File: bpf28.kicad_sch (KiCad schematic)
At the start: 39 parts

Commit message: 部品定数を入力　ただし未評価
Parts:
- C101, C130: value 10p -> NM
- C102, C129: value 10p -> 4700p
- C103, C105, C107, C109, C111, C113, C115, C117, C119, C121, C123, C125, C127: value 1p -> NM
- C104, C110, C126, C128: value 10p -> 330p
- C106, C120: value 10p -> 180p
- C114, C118: value 10p -> 150p
- L103, L105: value 10n -> NM
- L104, L106: value 1u -> 100n
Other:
- note added: "3t D8.0mm L2.1mm"
- note added: "Butterworth 24M-34M 171p, 79p, 197p"
- company: (none) -> JK1MLY / PRUG
- title: (none) -> FM QRP TRCV

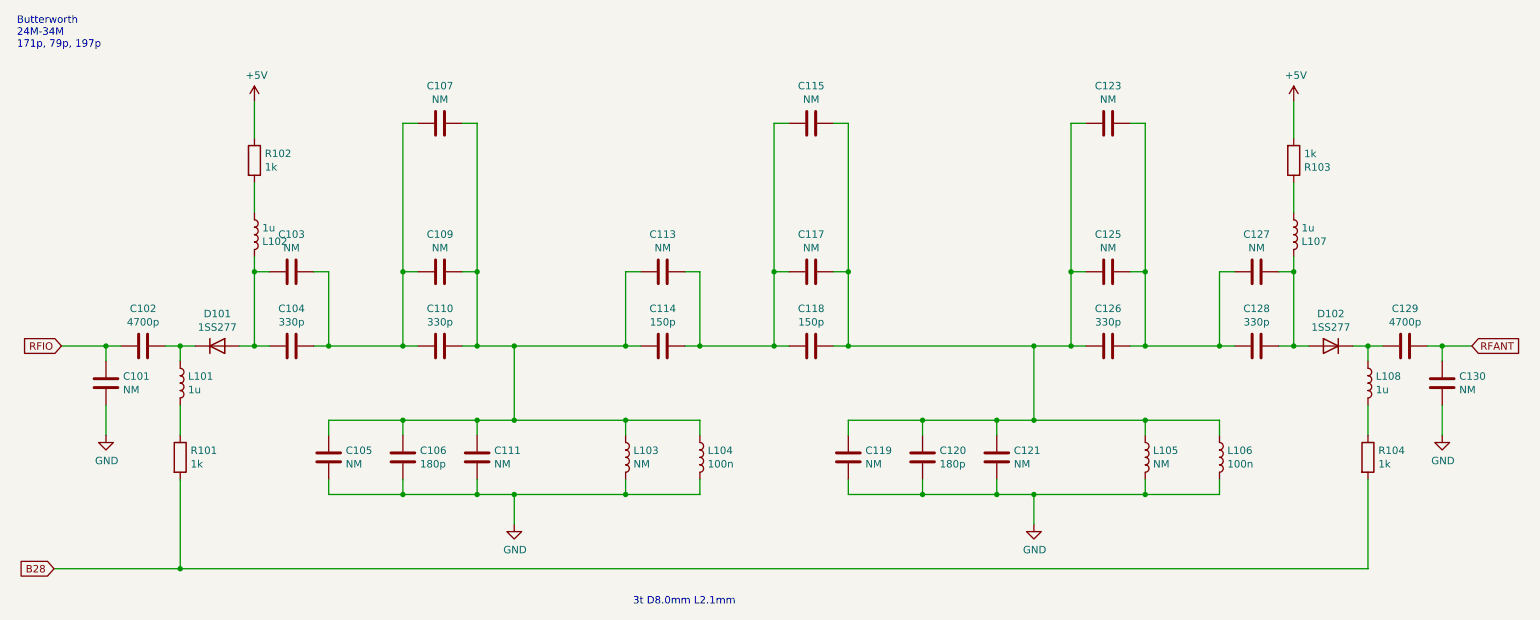
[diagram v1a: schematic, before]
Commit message: Add files via upload
フィルタ回路変更とジャンパクリーン
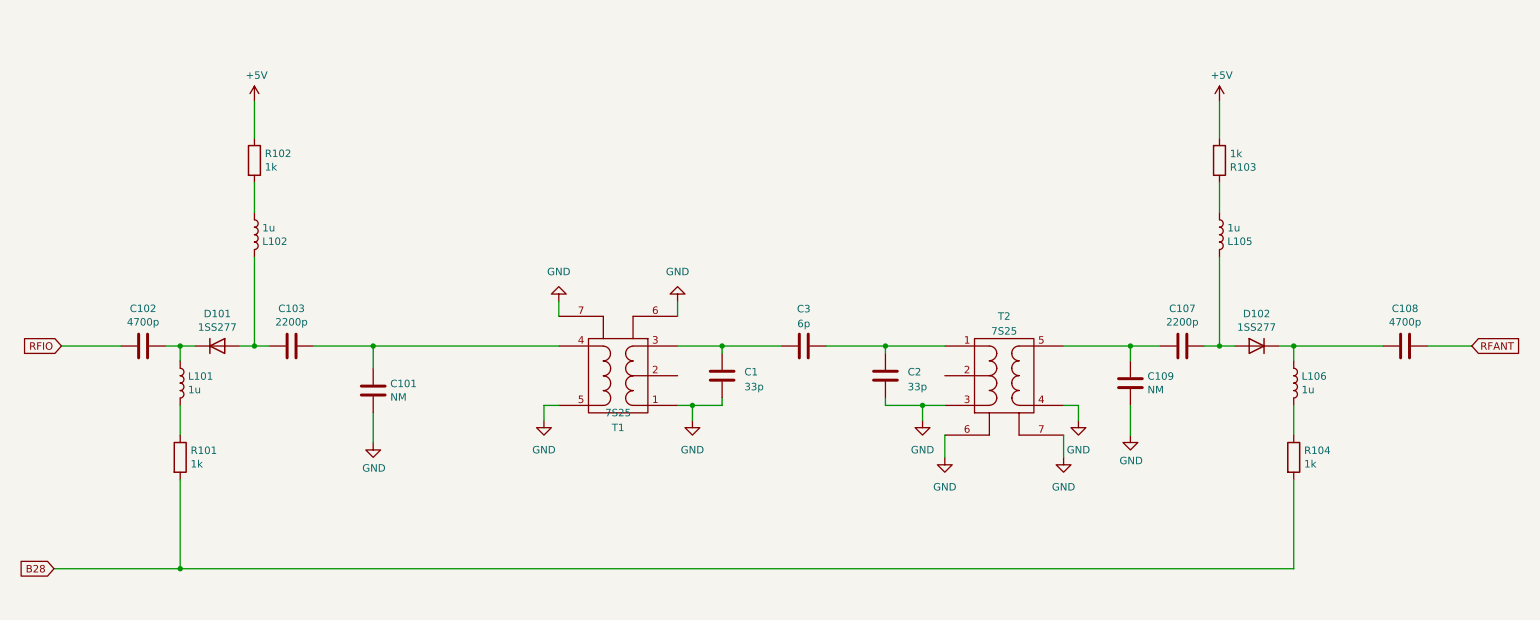
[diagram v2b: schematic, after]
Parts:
- removed C103, C105, C107, C109, C111, C113, C115, C117, C119, C121, C123, C125, C127: NM, digikey-footprints:0603, symbol Device:C
- removed C106, C120: 180p, Capacitor_THT:C_Disc_D3.4mm_W2.1mm_P2.50mm, symbol Device:C
- removed C110, C126: 330p, Capacitor_THT:C_Disc_D3.4mm_W2.1mm_P2.50mm, symbol Device:C
- removed C114, C118: 150p, Capacitor_THT:C_Disc_D3.4mm_W2.1mm_P2.50mm, symbol Device:C
- removed L103, L105: NM, Inductor_SMD:L_Murata_LQH2MCNxxxx02_2.0x1.6mm, symbol Device:L
- removed L104, L106: 100n, Resistor_THT:R_Axial_DIN0204_L3.6mm_D1.6mm_P5.08mm_Horizontal, symbol Device:L
- added C1, C2: 33p, Capacitor_THT:C_Disc_D3.0mm_W2.0mm_P2.50mm, symbol Device:C
- added C3: 6p, Capacitor_THT:C_Disc_D3.0mm_W2.0mm_P2.50mm, symbol Device:C
- added T1, T2: 7S25, usr-Library:coil_7mm, symbol Usr_Library:Transformer_SP_1S
- C103: renamed from C104; value 330p -> 2200p
- C107: renamed from C128; value 330p -> 2200p
- renumbered C129 to C108, C130 to C109, L107 to L105, L108 to L106
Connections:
- net GND: now also C1.2, C2.2, T1.1 (PR1), T1.5 (S2), T1.6 (G1), T1.7 (G2), T2.3 (PR2), T2.4 (S1), T2.6 (G1), T2.7 (G2)
- net RFANT: no longer C109.1
- net RFIO: no longer C101.1
- net at C103.2: now also C101.1, T1.4 (S1)
- net at C107.1: now also C109.1, T2.5 (S2)
- new net: C2.1, C3.1, T2.1 (PR1)
- new net: C1.1, C3.2, T1.3 (PR2)
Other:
- note removed: "3t D8.0mm L2.1mm"
- note removed: "Butterworth 24M-34M 171p, 79p, 197p"
- moved on the sheet: C101, C107, C109, D102, L105, L106, R103, R104

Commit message: アップデート
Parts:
- added R105: 1k, Resistor_THT:R_Axial_DIN0207_L6.3mm_D2.5mm_P2.54mm_Vertical, symbol Device:R
- D101, D102: footprint Diode_THT:D_A-405_P2.54mm_Vertical_AnodeUp -> Diode_THT:D_T-1_P5.08mm_Horizontal
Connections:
- net +5V: now also R103.1, R105.1; no longer R103.2
- net B28: now also R105.2
- net at L105.2: now also R103.2; no longer R103.1
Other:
- note added: "100p 7.5T 100p 560p 100p 7.5T 100p"
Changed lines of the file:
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@@
   (junction (at 228.6 76.2) (diameter 0) (color 0 0 0 0)
   )
+  (junction (at 39.37 114.3) (diameter 0) (color 0 0 0 0)
+  )
   (junction (at 138.43 86.36) (diameter 0) (color 0 0 0 0)
   )
@@
     (stroke (width 0) (type default))
   )
+  (wire (pts (xy 39.37 95.25) (xy 39.37 101.6))
+    (stroke (width 0) (type default))
+  )
   (wire (pts (xy 177.8 86.36) (xy 177.8 88.9))
     (stroke (width 0) (type default))
@@
     (stroke (width 0) (type default))
   )
+  (wire (pts (xy 39.37 109.22) (xy 39.37 114.3))
+    (stroke (width 0) (type default))
+  )
   (wire (pts (xy 135.89 68.58) (xy 135.89 71.12))
     (stroke (width 0) (type default))
@@
     (stroke (width 0) (type default))
   )
+  (wire (pts (xy 39.37 114.3) (xy 29.21 114.3))
+    (stroke (width 0) (type default))
+  )
   (wire (pts (xy 143.51 76.2) (xy 153.67 76.2))
     (stroke (width 0) (type default))
@@
     (stroke (width 0) (type default))
   )
-  (wire (pts (xy 50.8 114.3) (xy 29.21 114.3))
+  (wire (pts (xy 50.8 114.3) (xy 39.37 114.3))
     (stroke (width 0) (type default))
   )
@@
   (wire (pts (xy 241.3 76.2) (xy 241.3 78.74))
     (stroke (width 0) (type default))
+  )
+  (text "100p 7.5T 100p 560p 100p 7.5T 100p" (at 118.11 45.72 0)
+    (effects (font (size 1.27 1.27)) (justify left bottom))
   )
   (global_label "B28" (shape input) (at 29.21 114.3 180) (fields_autoplaced)
@@
       (effects (font (size 1.27 1.27)))
     )
-    (property "Footprint" "Diode_THT:D_A-405_P2.54mm_Vertical_AnodeUp" (at 57.15 76.2 0)
+    (property "Footprint" "Diode_THT:D_T-1_P5.08mm_Horizontal" (at 57.15 76.2 0)
       (effects (font (size 1.27 1.27)) hide)
     )
@@
       (effects (font (size 1.27 1.27)))
     )
-    (property "Footprint" "Diode_THT:D_A-405_P2.54mm_Vertical_AnodeUp" (at 234.95 76.2 0)
+    (property "Footprint" "Diode_THT:D_T-1_P5.08mm_Horizontal" (at 234.95 76.2 0)
       (effects (font (size 1.27 1.27)) hide)
     )
@@
     )
   )
-  (symbol (lib_id "Device:R") (at 228.6 44.45 0) (mirror x) (unit 1)
-    (in_bom yes) (on_board yes) (dnp no)
-    (property "Reference" "R103" (at 230.378 45.6184 0)
-      (effects (font (size 1.27 1.27)) (justify left))
-    )
-    (property "Value" "1k" (at 230.378 43.307 0)
-      (effects (font (size 1.27 1.27)) (justify left))
-    )
-    (property "Footprint" "Resistor_THT:R_Axial_DIN0207_L6.3mm_D2.5mm_P2.54mm_Vertical" (at 226.822 44.45 90)
+  (symbol (lib_id "Device:R") (at 228.6 44.45 0) (mirror y) (unit 1)
+    (in_bom yes) (on_board yes) (dnp no)
+    (property "Reference" "R103" (at 226.822 43.2816 0)
+      (effects (font (size 1.27 1.27)) (justify left))
+    )
+    (property "Value" "1k" (at 226.822 45.593 0)
+      (effects (font (size 1.27 1.27)) (justify left))
+    )
+    (property "Footprint" "Resistor_THT:R_Axial_DIN0207_L6.3mm_D2.5mm_P2.54mm_Vertical" (at 230.378 44.45 90)
       (effects (font (size 1.27 1.27)) hide)
     )
@@
         (path "/6d1d60ff-408a-47a7-892f-c5cf9ef6ca75/00000000-0000-0000-0000-000061d100f6"
           (reference "#PWR0110") (unit 1)
+        )
+      )
+    )
+  )
+  (symbol (lib_id "power:+5V") (at 39.37 95.25 0) (unit 1)
+    (in_bom yes) (on_board yes) (dnp no)
+    (property "Reference" "#PWR054" (at 39.37 99.06 0)
+      (effects (font (size 1.27 1.27)) hide)
+    )
+    (property "Value" "+5V" (at 39.751 90.8558 0)
+      (effects (font (size 1.27 1.27)))
+    )
+    (property "Footprint" "" (at 39.37 95.25 0)
+      (effects (font (size 1.27 1.27)) hide)
+    )
+    (property "Datasheet" "" (at 39.37 95.25 0)
+      (effects (font (size 1.27 1.27)) hide)
+    )
+    (pin "1")
+    (instances
+      (project "fm_qrp2"
+        (path "/6d1d60ff-408a-47a7-892f-c5cf9ef6ca75/00000000-0000-0000-0000-000061d100f6"
+          (reference "#PWR054") (unit 1)
         )
       )
@@
         )
       )
+    )
+  )
+  (symbol (lib_id "Device:R") (at 39.37 105.41 0) (unit 1)
+    (in_bom yes) (on_board yes) (dnp no)
+    (property "Reference" "R105" (at 41.148 104.2416 0)
+      (effects (font (size 1.27 1.27)) (justify left))
+    )
+    (property "Value" "1k" (at 41.148 106.553 0)
+      (effects (font (size 1.27 1.27)) (justify left))
+    )
+    (property "Footprint" "Resistor_THT:R_Axial_DIN0207_L6.3mm_D2.5mm_P2.54mm_Vertical" (at 37.592 105.41 90)
+      (effects (font (size 1.27 1.27)) hide)
+    )
+    (property "Datasheet" "~" (at 39.37 105.41 0)
+      (effects (font (size 1.27 1.27)) hide)
+    )
+    (pin "1")
+    (pin "2")
+    (instances
+      (project "fm_qrp2"
+        (path "/6d1d60ff-408a-47a7-892f-c5cf9ef6ca75/00000000-0000-0000-0000-000061d100f6"
+          (reference "R105") (unit 1)
+        )
+      )

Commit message: Add files via upload
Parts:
- C1, C2: value 33p -> 24p
- C102, C108: value 4700p -> 0.01u
- C103, C107: value 2200p -> 0.01u
- C3: value 6p -> 4p
- L101, L102, L105, L106: value 1u -> 10u
- R101, R102, R103, R104: value 1k -> 470
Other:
- note added: "L203,204はFCZ 7S25相当 サトー電気で入手可能"
- note removed: "100p 7.5T 100p 560p 100p 7.5T 100p"
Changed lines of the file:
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@@
   (title_block
     (title "FM QRP TRCV")
-    (date "2022-03-12")
+    (date "2023-08-12")
     (rev "1")
     (company "JK1MLY / PRUG")
@@
     (stroke (width 0) (type default))
   )
-  (text "100p 7.5T 100p 560p 100p 7.5T 100p" (at 118.11 45.72 0)
+  (text "L203,204はFCZ 7S25相当\nサトー電気で入手可能" (at 123.19 52.07 0)
     (effects (font (size 1.27 1.27)) (justify left bottom))
   )
@@
       (effects (font (size 1.27 1.27)) (justify left))
     )
-    (property "Value" "1u" (at 242.6462 83.693 0)
+    (property "Value" "10u" (at 242.6462 83.693 0)
       (effects (font (size 1.27 1.27)) (justify left))
     )
@@
       (effects (font (size 1.27 1.27)) (justify left))
     )
-    (property "Value" "1k" (at 65.278 45.593 0)
+    (property "Value" "470" (at 65.278 45.593 0)
       (effects (font (size 1.27 1.27)) (justify left))
     )
@@
       (effects (font (size 1.27 1.27)) hide)
     )
-    (property "Datasheet" "~" (at 63.5 44.45 0)
+    (property "Datasheet" "R-25471" (at 63.5 44.45 0)
       (effects (font (size 1.27 1.27)) hide)
     )
@@
       (effects (font (size 1.27 1.27)) (justify left))
     )
-    (property "Value" "1k" (at 243.078 96.393 0)
+    (property "Value" "470" (at 243.078 96.393 0)
       (effects (font (size 1.27 1.27)) (justify left))
     )
@@
       (effects (font (size 1.27 1.27)) hide)
     )
-    (property "Datasheet" "~" (at 241.3 95.25 0)
+    (property "Datasheet" "R-25471" (at 241.3 95.25 0)
       (effects (font (size 1.27 1.27)) hide)
     )
@@
       (effects (font (size 1.27 1.27)))
     )
-    (property "Value" "2200p" (at 69.85 72.1106 90)
+    (property "Value" "0.01u" (at 69.85 72.1106 90)
       (effects (font (size 1.27 1.27)))
     )
@@
       (effects (font (size 1.27 1.27)) hide)
     )
-    (property "Datasheet" "~" (at 69.85 76.2 0)
+    (property "Datasheet" "sato" (at 69.85 76.2 0)
       (effects (font (size 1.27 1.27)) hide)
     )
@@
       (effects (font (size 1.27 1.27)))
     )
-    (property "Value" "2200p" (at 222.25 72.1106 90)
+    (property "Value" "0.01u" (at 222.25 72.1106 90)
       (effects (font (size 1.27 1.27)))
     )
@@
       (effects (font (size 1.27 1.27)) hide)
     )
-    (property "Datasheet" "~" (at 222.25 76.2 0)
+    (property "Datasheet" "sato" (at 222.25 76.2 0)
       (effects (font (size 1.27 1.27)) hide)
     )
@@
       (effects (font (size 1.27 1.27)) (justify left))
     )
-    (property "Value" "1u" (at 52.1462 83.693 0)
+    (property "Value" "10u" (at 52.1462 83.693 0)
       (effects (font (size 1.27 1.27)) (justify left))
     )
@@
       (effects (font (size 1.27 1.27)) (justify left))
     )
-    (property "Value" "1k" (at 52.578 96.393 0)
+    (property "Value" "470" (at 52.578 96.393 0)
       (effects (font (size 1.27 1.27)) (justify left))
     )
@@
       (effects (font (size 1.27 1.27)) hide)
     )
-    (property "Datasheet" "~" (at 50.8 95.25 0)
+    (property "Datasheet" "R-25471" (at 50.8 95.25 0)
       (effects (font (size 1.27 1.27)) hide)
     )
@@
       (effects (font (size 1.27 1.27)) (justify left))
     )
-    (property "Value" "1u" (at 64.8462 56.007 0)
+    (property "Value" "10u" (at 64.8462 56.007 0)
       (effects (font (size 1.27 1.27)) (justify left))
     )
@@
       (effects (font (size 1.27 1.27)) (justify left))
     )
-    (property "Value" "1k" (at 226.822 45.593 0)
+    (property "Value" "470" (at 226.822 45.593 0)
       (effects (font (size 1.27 1.27)) (justify left))
     )
@@
       (effects (font (size 1.27 1.27)) hide)
     )
-    (property "Datasheet" "~" (at 228.6 44.45 0)
+    (property "Datasheet" "R-25471" (at 228.6 44.45 0)
       (effects (font (size 1.27 1.27)) hide)
     )
@@
       (effects (font (size 1.27 1.27)) (justify left))
     )
-    (property "Value" "1u" (at 229.9462 56.007 0)
+    (property "Value" "10u" (at 229.9462 56.007 0)
       (effects (font (size 1.27 1.27)) (justify left))
     )
@@
       (effects (font (size 1.27 1.27)))
     )
-    (property "Value" "4700p" (at 260.35 72.1106 90)
+    (property "Value" "0.01u" (at 260.35 72.1106 90)
       (effects (font (size 1.27 1.27)))
     )
@@
       (effects (font (size 1.27 1.27)) hide)
     )
-    (property "Datasheet" "~" (at 260.35 76.2 0)
+    (property "Datasheet" "sato" (at 260.35 76.2 0)
       (effects (font (size 1.27 1.27)) hide)
     )
@@
       (effects (font (size 1.27 1.27)))
     )
-    (property "Value" "4700p" (at 44.45 72.1106 90)
+    (property "Value" "0.01u" (at 44.45 72.1106 90)
       (effects (font (size 1.27 1.27)))
     )
@@
       (effects (font (size 1.27 1.27)) hide)
     )
-    (property "Datasheet" "~" (at 44.45 76.2 0)
+    (property "Datasheet" "sato" (at 44.45 76.2 0)
       (effects (font (size 1.27 1.27)) hide)
     )
@@
       (effects (font (size 1.27 1.27)) (justify left))
     )
-    (property "Value" "33p" (at 175.26 83.185 0)
+    (property "Value" "24p" (at 175.26 83.185 0)
       (effects (font (size 1.27 1.27)) (justify left))
     )
@@
       (effects (font (size 1.27 1.27)) hide)
     )
-    (property "Datasheet" "~" (at 171.45 81.28 0)
+    (property "Datasheet" "sato" (at 171.45 81.28 0)
       (effects (font (size 1.27 1.27)) hide)
     )
@@
       (effects (font (size 1.27 1.27)))
     )
-    (property "Value" "6p" (at 157.48 72.39 90)
+    (property "Value" "4p" (at 157.48 72.39 90)
       (effects (font (size 1.27 1.27)))
     )
@@
       (effects (font (size 1.27 1.27)) hide)
     )
-    (property "Datasheet" "~" (at 157.48 76.2 0)
+    (property "Datasheet" "sato" (at 157.48 76.2 0)
       (effects (font (size 1.27 1.27)) hide)
     )
@@
       (effects (font (size 1.27 1.27)) hide)
     )
-    (property "Datasheet" "~" (at 191.77 81.28 0)
+    (property "Datasheet" "sato" (at 191.77 81.28 0)
       (effects (font (size 1.27 1.27)) hide)
     )
@@
       (effects (font (size 1.27 1.27)))
     )
-    (property "Value" "7S25" (at 125.7173 87.63 0)
+    (property "Value" "7S25" (at 125.73 92.71 0)
       (effects (font (size 1.27 1.27)))
     )
@@
       (effects (font (size 1.27 1.27)) hide)
     )
-    (property "Datasheet" "~" (at 125.73 81.28 0)
+    (property "Datasheet" "sato" (at 125.73 81.28 0)
       (effects (font (size 1.27 1.27)) hide)
     )
@@
       (effects (font (size 1.27 1.27)) (justify left))
     )
-    (property "Value" "33p" (at 147.32 83.185 0)
+    (property "Value" "24p" (at 147.32 83.185 0)
       (effects (font (size 1.27 1.27)) (justify left))
     )
@@
       (effects (font (size 1.27 1.27)) hide)
     )
-    (property "Datasheet" "~" (at 143.51 81.28 0)
+    (property "Datasheet" "sato" (at 143.51 81.28 0)
       (effects (font (size 1.27 1.27)) hide)
     )
@@
       (effects (font (size 1.27 1.27)) hide)
     )
-    (property "Datasheet" "~" (at 39.37 105.41 0)
-      (effects (font (size 1.27 1.27)) hide)
-    )
+    (property "Datasheet" "R-25102" (at 39.37 105.41 0)
+      (effects (font (size 1.27 1.27)) hide)
+    )
